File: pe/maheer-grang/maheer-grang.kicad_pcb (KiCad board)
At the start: 2 copper layers, 10.5 x 16.5 mm, 12 parts, among them U1 AP62300TWU

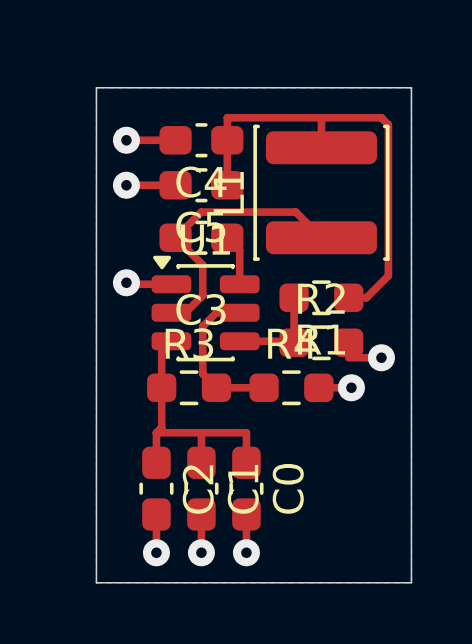
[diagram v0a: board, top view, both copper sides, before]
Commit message: updated the buck schematic (added digikey PN/links and 1 more output cap)
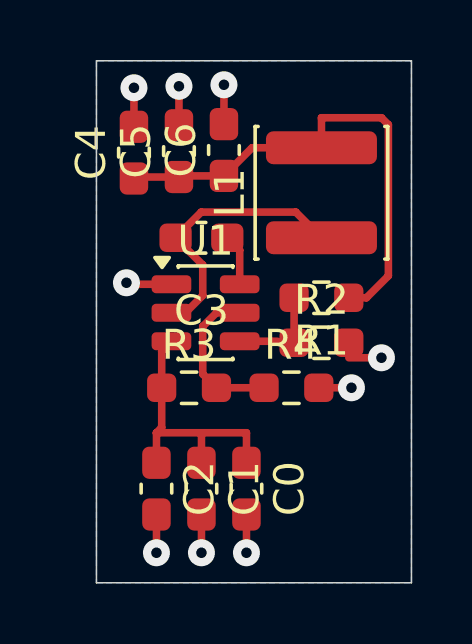
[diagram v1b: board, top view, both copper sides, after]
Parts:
- added C6: 22 µF, Capacitor_SMD:C_0603_1608Metric_Pad1.08x0.95mm_HandSolder, F.Cu at (139.8, 82.6)
- moved C4 2.29 mm to (136.8, 82.7), turned to 90 degrees
- moved C5 1.36 mm to (138.2, 82.6), turned to 90 degrees
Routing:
- net Net-(C4-Pad1): track 15.4 -> 16.7 mm
- net GNDREF: track 10.9 -> 11.5 mm, vias 8 -> 9
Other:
- board size 10.5 x 16.5 mm -> 10.5 x 17.4 mm
